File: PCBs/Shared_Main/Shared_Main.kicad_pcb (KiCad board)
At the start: 4 copper layers, 175.3 x 61 mm, 49 parts, among them J1 Power, J10 Digital inputs, J11 Digital inputs, J12 Digital inputs, J13 Digital inputs, J14 Digital inputs, J15 Digital inputs, J16 Other unit, J2 Screw_Terminal_01x04, J4 Aux, J5 Analog inputs, J7 Keypad, Q1 BC547, Q2 BC547, Q3 BC547, Q4 BC547, U1 ESP32-S3-ZERO, U2 74HC4051, U4 74HC165, U5 74HC165, U6 74HC165, U7 74HC165, U8 74HC165, U9 74HC165

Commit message: tweaks
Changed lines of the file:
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@@
 	)
 	(segment
-		(start 171.45 85.09)
-		(end 166.37 80.01)
+		(start 168.91 82.55)
+		(end 171.45 85.09)
 		(width 0.25)
 		(layer "F.Cu")
@@
 	)
 	(segment
-		(start 166.37 80.01)
-		(end 166.37 79.375)
+		(start 166.37 79.375)
+		(end 168.91 81.915)
 		(width 0.25)
 		(layer "F.Cu")
+		(net "Net-(Q1-B)")
+	)
+	(segment
+		(start 168.91 81.915)
+		(end 168.91 82.55)
+		(width 0.25)
+		(layer "F.Cu")

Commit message: silkscreen labels and tweaks
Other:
- board text added: "A0"
- board text added: "A7"
- board text added: "BC547"
- board text added: "D00"
- board text added: "D08"
- board text added: "D16"
- board text added: "D24"
- board text added: "D32"
- board text added: "D40"
- board text added: "GND or High-Z"
- board text removed: "0"
- board text removed: "16"
- board text removed: "24"
- board text removed: "32"
- board text removed: "40"
- board text removed: "8"

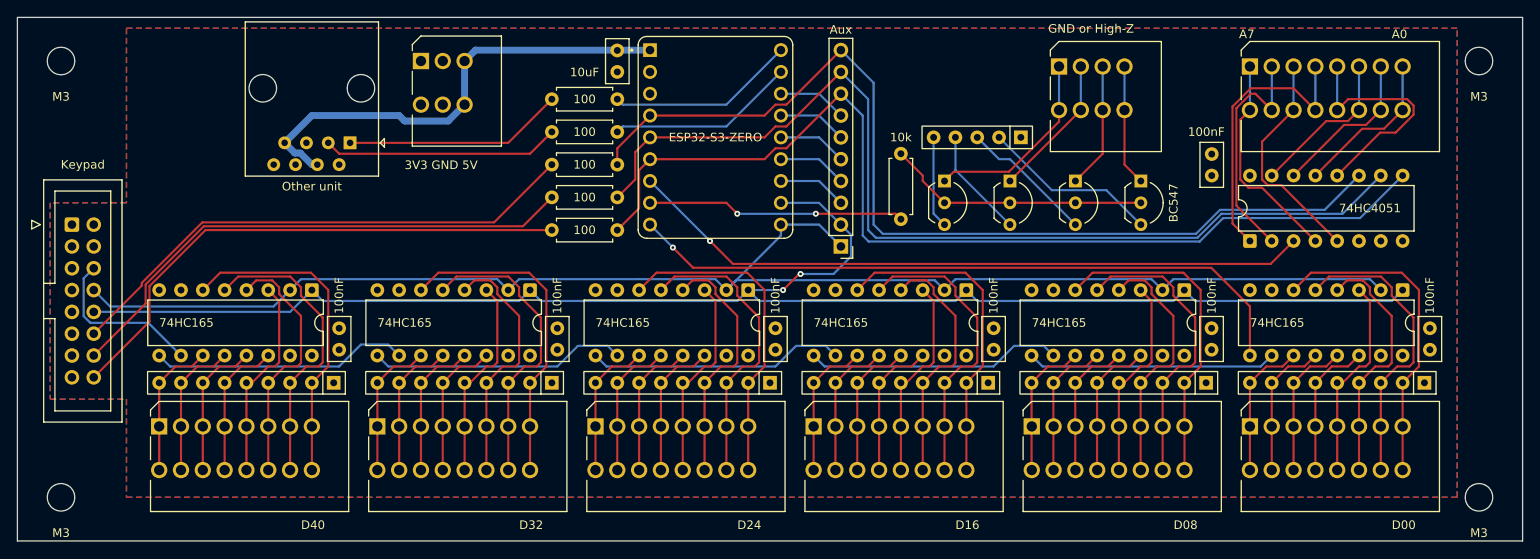
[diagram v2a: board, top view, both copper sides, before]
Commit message: fix aisler sync (new projects)
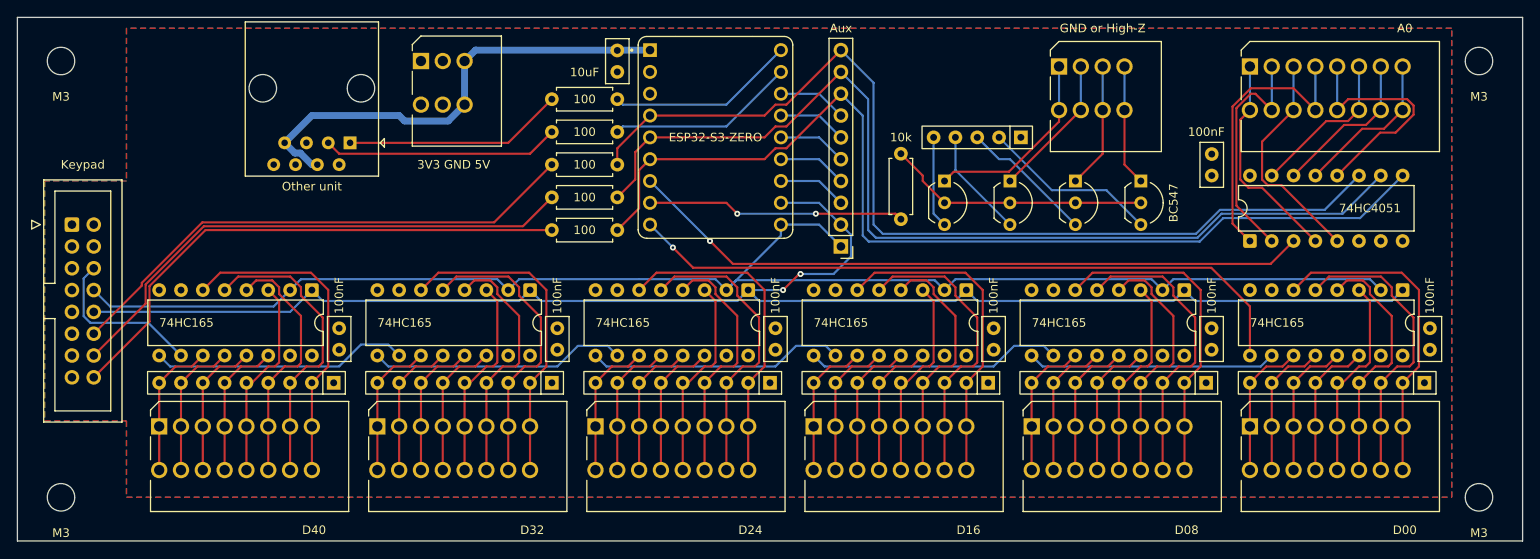
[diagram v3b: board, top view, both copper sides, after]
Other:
- board text removed: "A7"
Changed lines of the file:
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@@
 	(paper "A4")
 	(title_block
-		(comment 4 "AISLER Project ID: YKPHGLFW")
+		(comment 4 "AISLER Project ID: QEYRPUHY")
 	)
 	(layers
@@
 		)
 		(property "Value" "Aux"
-			(at 0 25.24 0)
+			(at 0 25.4 0)
 			(layer "F.SilkS")
 			(effects
@@
 	)
 	(gr_text "D40"
-		(at 96.52 123.19 0)
+		(at 98.044 123.19 0)
 		(layer "F.SilkS")
 		(effects
@@
 				(thickness 0.15)
 			)
-			(justify left bottom)
 		)
 	)
 	(gr_text "3V3 GND 5V"
-		(at 108.585 81.28 0)
+		(at 114.3 80.645 0)
 		(layer "F.SilkS")
 		(effects
@@
 				(thickness 0.15)
 			)
-			(justify left bottom)
 		)
 	)
 	(gr_text "D32"
-		(at 121.92 123.19 0)
+		(at 123.444 123.19 0)
 		(layer "F.SilkS")
 		(effects
@@
 				(thickness 0.15)
 			)
-			(justify left bottom)
 		)
 	)
 	(gr_text "D24"
-		(at 147.32 123.19 0)
+		(at 148.844 123.19 0)
 		(layer "F.SilkS")
 		(effects
@@
 				(thickness 0.15)
 			)
-			(justify left bottom)
 		)
 	)
 	(gr_text "D16"
-		(at 172.72 123.19 0)
+		(at 174.244 123.19 0)
 		(layer "F.SilkS")
 		(effects
@@
 				(thickness 0.15)
 			)
-			(justify left bottom)
 		)
 	)
 	(gr_text "GND or High-Z"
-		(at 183.515 65.405 0)
+		(at 189.865 64.77 0)
 		(layer "F.SilkS")
 		(effects
@@
 				(thickness 0.15)
 			)
-			(justify left bottom)
 		)
 	)
 	(gr_text "D08"
-		(at 198.12 123.19 0)
+		(at 199.644 123.19 0)
 		(layer "F.SilkS")
 		(effects
@@
 				(thickness 0.15)
 			)
-			(justify left bottom)
-		)
-	)
-	(gr_text "A7"
-		(at 205.74 66.04 0)
-		(layer "F.SilkS")
-		(effects
-			(font
-				(size 1 1)
-				(thickness 0.15)
-			)
-			(justify left bottom)
 		)
 	)
 	(gr_text "A0"
-		(at 223.52 66.04 0)
+		(at 225.044 64.77 0)
 		(layer "F.SilkS")
 		(effects
@@
 				(thickness 0.15)
 			)
-			(justify left bottom)
 		)
 	)
 	(gr_text "D00"
-		(at 223.52 123.19 0)
+		(at 225.044 123.19 0)
 		(layer "F.SilkS")
 		(effects
@@
 				(thickness 0.15)
 			)
-			(justify left bottom)
 		)
 	)
@@
 		(polygon
 			(pts
-				(xy 76.2 64.77) (xy 76.2 85.09) (xy 67.31 85.09) (xy 67.31 107.95) (xy 76.2 107.95) (xy 76.2 119.38)
-				(xy 231.14 119.38) (xy 231.14 64.77)
+				(xy 76.2 64.77) (xy 76.2 82.55) (xy 66.675 82.55) (xy 66.675 110.49) (xy 76.2 110.49) (xy 76.2 119.38)
+				(xy 230.505 119.38) (xy 230.505 64.77)
 			)
 		)
@@
 		(polygon
 			(pts
-				(xy 76.2 64.77) (xy 76.2 85.09) (xy 67.31 85.09) (xy 67.31 107.95) (xy 76.2 107.95) (xy 76.2 119.38)
-				(xy 231.14 119.38) (xy 231.14 64.77)
+				(xy 76.2 64.77) (xy 76.2 82.55) (xy 66.675 82.55) (xy 66.675 110.49) (xy 76.2 110.49) (xy 76.2 119.38)
+				(xy 230.505 119.38) (xy 230.505 64.77)
 			)
 		)
@@
 		(polygon
 			(pts
-				(xy 76.2 85.09) (xy 67.31 85.09) (xy 67.31 107.95) (xy 76.2 107.95) (xy 76.2 119.38) (xy 231.14 119.38)
-				(xy 231.14 64.77) (xy 76.2 64.77)
+				(xy 76.2 82.55) (xy 66.675 82.55) (xy 66.675 110.49) (xy 76.2 110.49) (xy 76.2 119.38) (xy 230.505 119.38)
+				(xy 230.505 64.77) (xy 76.2 64.77)
 			)
 		)
@@
 		(polygon
 			(pts
-				(xy 76.2 85.09) (xy 67.31 85.094379) (xy 67.31 107.95) (xy 76.2 107.95) (xy 76.2 119.38) (xy 231.14 119.38)
-				(xy 231.14 64.77) (xy 76.2 64.77)
+				(xy 76.2 82.547809) (xy 66.675 82.552502) (xy 66.675 110.49) (xy 76.2 110.49) (xy 76.2 119.38) (xy 230.505 119.38)
+				(xy 230.505 64.77) (xy 76.2 64.77)
 			)
 		)

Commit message: revert to horizontal screw terminals to save cost
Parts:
- J1: footprint Custom_Footprints:SpringTerminal_1x03_P2.54mm_Vertical -> TerminalBlock_Phoenix:TerminalBlock_Phoenix_MKDS-1,5-3_1x03_P5.00mm_Horizontal
- J10, J11, J12, J13, J14, J15, J5: footprint Custom_Footprints:SpringTerminal_1x08_P2.54mm_Vertical -> TerminalBlock_Phoenix:TerminalBlock_Phoenix_MPT-0,5-8-2.54_1x08_P2.54mm_Horizontal
- J2: value Screw_Terminal_01x04 -> GND or High-Z; footprint Custom_Footprints:SpringTerminal_1x04_P2.54mm_Vertical -> TerminalBlock_Phoenix:TerminalBlock_Phoenix_MPT-0,5-4-2.54_1x04_P2.54mm_Horizontal
- moved Q1 22.9 mm to (171.4, 82.5)
- moved Q4 22.9 mm to (194.3, 82.5)
- moved J5 19.3 mm to (224.8, 76.8), turned to 180 degrees
- moved J1 16.8 mm to (120.7, 81.9), turned to 180 degrees
- moved J2 12.2 mm to (194.3, 76.8), turned to 180 degrees
- moved RN8 10.2 mm to (170.2, 78.7), turned to 0 degrees
- moved Q2 7.62 mm to (179.1, 82.5)
- moved Q3 7.62 mm to (186.7, 82.5)
- moved H2 6.35 mm to (233.7, 113.0)
- moved H3 6.35 mm to (68.6, 113.0)
- moved C1 5.08 mm to (203.2, 84.5), turned to 90 degrees
- moved C2 3.56 mm to (130.8, 67.3), turned to 0 degrees
- moved J7 2.54 mm to (69.8, 85.1)
- moved J10 0.64 mm to (207.0, 111.8)
- moved J11 0.64 mm to (181.6, 111.8)
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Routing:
- net Net-(J5-Pin_5): track 27.7 -> 6.13 mm
- net Net-(J2-Pin_1): track 22.6 -> 5.72 mm
- net Net-(J5-Pin_4): track 33.2 -> 16.9 mm
- net Net-(J5-Pin_7): track 18.4 -> 6.13 mm
- net Net-(Q1-E): track 20.7 -> 9.42 mm
- net Net-(J5-Pin_2): track 27.9 -> 18.9 mm
- net Net-(J2-Pin_2): track 16.8 -> 7.82 mm
- net Net-(J5-Pin_8): track 18.4 -> 9.72 mm
- net Net-(J5-Pin_1): track 25.3 -> 16.9 mm
- net Net-(Q4-E): track 10.7 -> 17.7 mm
- net Net-(Q2-E): track 16.0 -> 10.5 mm
- net Net-(J14-Pin_7): track 34.8 -> 29.7 mm
- net Net-(J13-Pin_8): track 38.0 -> 33.0 mm
- net Net-(J13-Pin_6): track 29.4 -> 24.3 mm
- net Net-(J13-Pin_7): track 34.8 -> 29.7 mm
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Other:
- board size 175.3 x 61 mm -> 175.3 x 54.6 mm
- board text added: "5V GND 3V3"
- board text removed: "3V3 GND 5V"

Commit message: stuff
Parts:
- C2: footprint Capacitor_THT:C_Disc_D5.0mm_W2.5mm_P2.50mm -> Capacitor_THT:C_Disc_D6.0mm_W4.4mm_P5.00mm
- moved C2 2.50 mm to (128.3, 67.3)

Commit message: Fixed issues identified by Claude - batch 1
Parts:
- removed RN8: R_Network04, Resistor_THT:R_Array_SIP5
- added C3: 100uF, Capacitor_THT:CP_Radial_D5.0mm_P2.00mm, F.Cu at (103.5, 85.0)
- added F1: 0.5A, Fuse:Fuse_Bourns_MF-RHT050, F.Cu at (91.4, 86.4)
- added R7: 10k, Resistor_THT:R_Axial_DIN0207_L6.3mm_D2.5mm_P7.62mm_Horizontal, F.Cu at (166.4, 75.6)
- added R8: 10k, Resistor_THT:R_Axial_DIN0207_L6.3mm_D2.5mm_P7.62mm_Horizontal, F.Cu at (78.7, 83.8)
- J2: value GND or High-Z -> GND or Floating
- moved J16 6.98 mm to (95.2, 78.1)
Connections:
- J16 pad 4: +5V -> /+5V_RJ45
- J16 pad 7: +5V -> /+5V_RJ45
- Q1 pad 3: Net-(Q1-E) -> GND
- Q2 pad 3: Net-(Q2-E) -> GND
- Q3 pad 3: Net-(Q3-E) -> GND
- Q4 pad 3: Net-(Q4-E) -> GND
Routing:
- net Net-(Q4-E): track 17.7 -> 0.00 mm
- net Net-(Q3-E): track 12.6 -> 0.00 mm
- net /+5V_RJ45: track 0.00 -> 10.6 mm
- net Net-(Q2-E): track 10.5 -> 0.00 mm
- net Net-(Q1-E): track 9.42 -> 0.00 mm
- net /SR_Q7_KP: track 20.3 -> 29.3 mm, vias 0 -> 1
- net Net-(J16-FROM_B): track 27.5 -> 34.6 mm
- net Net-(J16-FROM_A): track 26.2 -> 33.2 mm
- net Net-(Q1-B): track 30.7 -> 34.5 mm
- net /SR_PL: track 184.4 -> 186.6 mm, vias 2 -> 4
- net +5V: track 51.2 -> 49.0 mm
- net /ADDR2_KP: track 60.3 -> 62.0 mm
- net /ADDR1_KP: track 60.7 -> 61.8 mm
